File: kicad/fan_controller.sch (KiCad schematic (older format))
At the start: 49 parts, among them P1 CONN_01X04, P2 CONN_01X05, P3 CONN_01X04, P4 CONN_01X04, P5 CONN_01X04, P6 CONN_01X04, Q1 Q_NPN_BEC, Q2 Q_NPN_BEC, Q3 Q_NPN_BEC, Q4 Q_NPN_BEC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

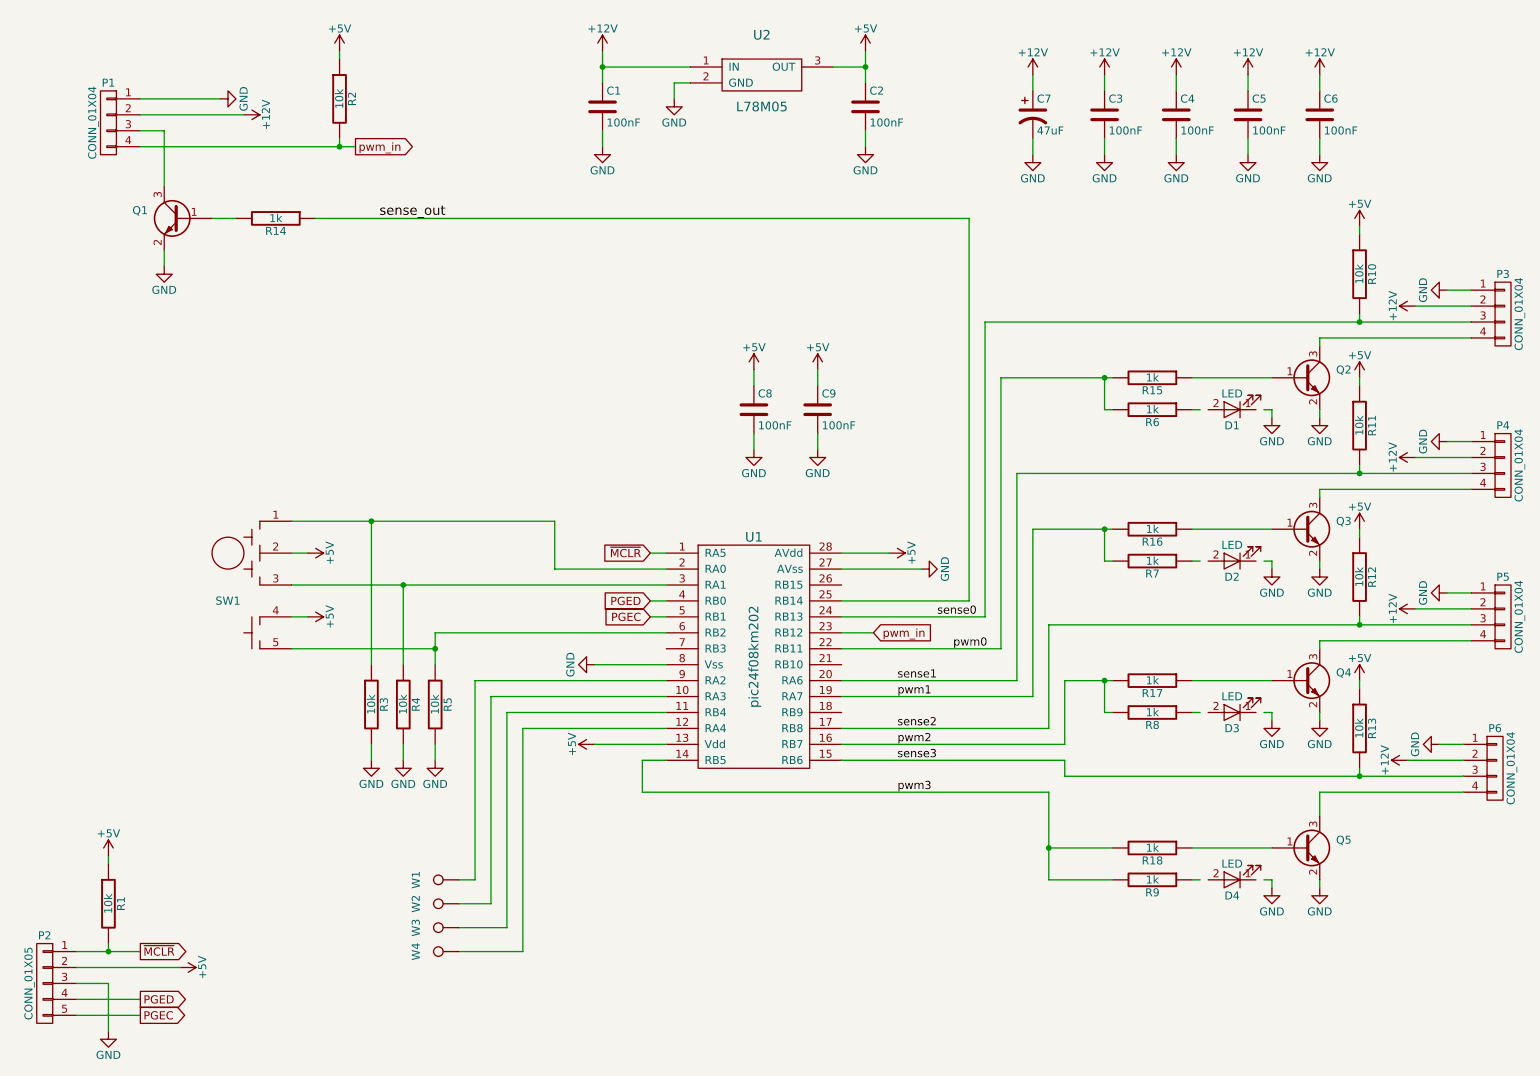
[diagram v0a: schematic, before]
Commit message: Added hardware files for v1.1 schematic and board
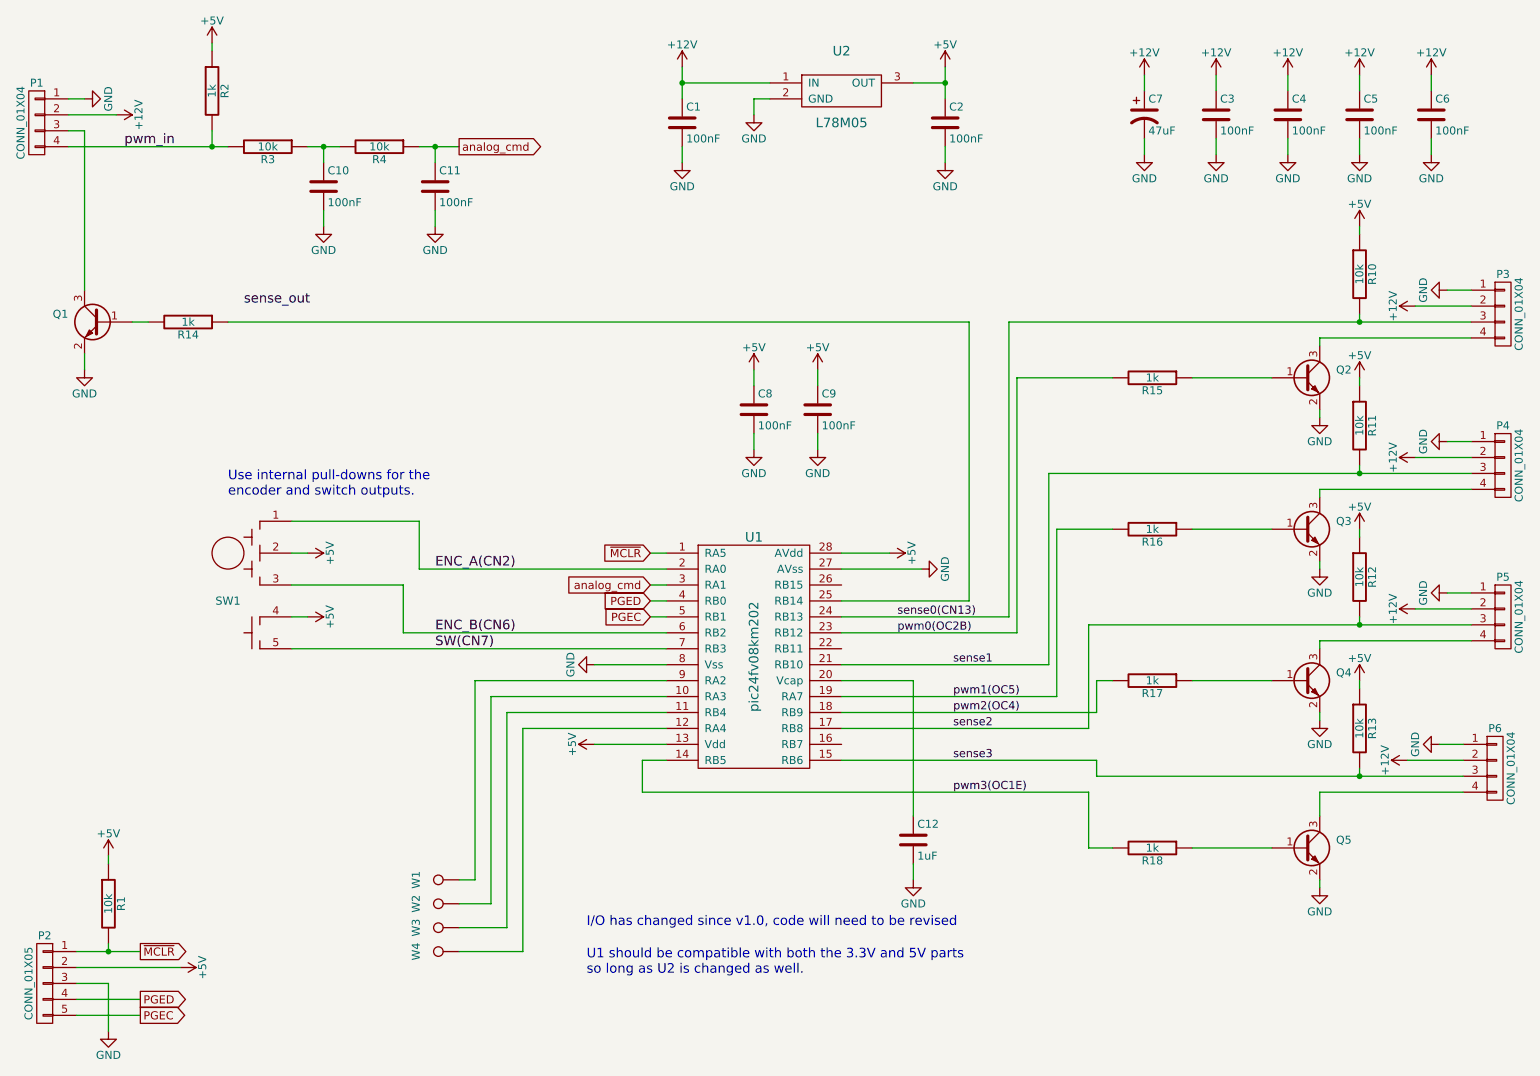
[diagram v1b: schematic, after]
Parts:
- removed D1, D2, D3, D4: LED, lib_pcb:led_0603, symbol LED
- removed R5: 10k, kicad_pcb:SM_0603, symbol R
- removed R6, R7, R8, R9: 1k, kicad_pcb:SM_0603, symbol R
- removed U1: pic24f08km202, kicad_pcb:SSOP-28, symbol pic24f08km202
- added C10, C11: 100nF, lib_pcb:SM_0603, symbol C
- added C12: 1uF, lib_pcb:SM_0603, symbol C
- added U1: pic24fv08km202, kicad_pcb:SSOP-28, symbol pic24fv08km202
- R2: value 10k -> 1k; Description resistor, 10k, 0603 -> resistor, 1k, 0603; MPN RC0603JR-0710KL -> RC0603JR-071KL
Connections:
- net labels added: ENC_A(CN2), ENC_B(CN6), SW(CN7), analog_cmd, pwm0(OC2B), pwm1(OC5), pwm2(OC4), pwm3(OC1E), sense0(CN13)
- net labels removed: pwm0, pwm1, pwm2, pwm3, sense0
- wire segments 153 -> 138
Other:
- note added: "I/O has changed since v1.0, code will need to be revised"
- note added: "U1 should be compatible with both the 3.3V and 5V parts\nso long as U2 is changed as well."
- note added: "Use internal pull-downs for the\nencoder and switch outputs."
- moved on the sheet: C1, C2, C3, C4, C5, C6, C7, P1, Q1, R14, U2

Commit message: Added missing BOM information
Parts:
- C12: Description (none) -> capacitor, ceramic, 1uF 16V; MPN (none) -> CC0603ZRY5V7BB105; Manufacturer (none) -> Yageo
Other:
- note added: "Add thermistor for temperature-controlled cooling?"
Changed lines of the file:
@@
 F 2 "lib_pcb:SM_0603" H 6438 5550 50  0001 C CNN
 F 3 "" H 6400 5700 50  0000 C CNN
+F 4 "CC0603ZRY5V7BB105" H 6400 5700 60  0001 C CNN "MPN"
+F 5 "Yageo" H 6400 5700 60  0001 C CNN "Manufacturer"
+F 6 "capacitor, ceramic, 1uF 16V" H 6400 5700 60  0001 C CNN "Description"
 	1    6400 5700
 	1    0    0    -1
@@
 Text Notes 2100 3550 0    60   ~ 0
 Use internal pull-downs for the\nencoder and switch outputs.
+Text Notes 900  4900 0    60   ~ 0
+Add thermistor for temperature-controlled cooling?
 $EndSCHEMATC
